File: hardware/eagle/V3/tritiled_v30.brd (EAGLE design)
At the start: 25.4 x 25.4 mm, 12 parts, among them IC1 PIC12LF1571

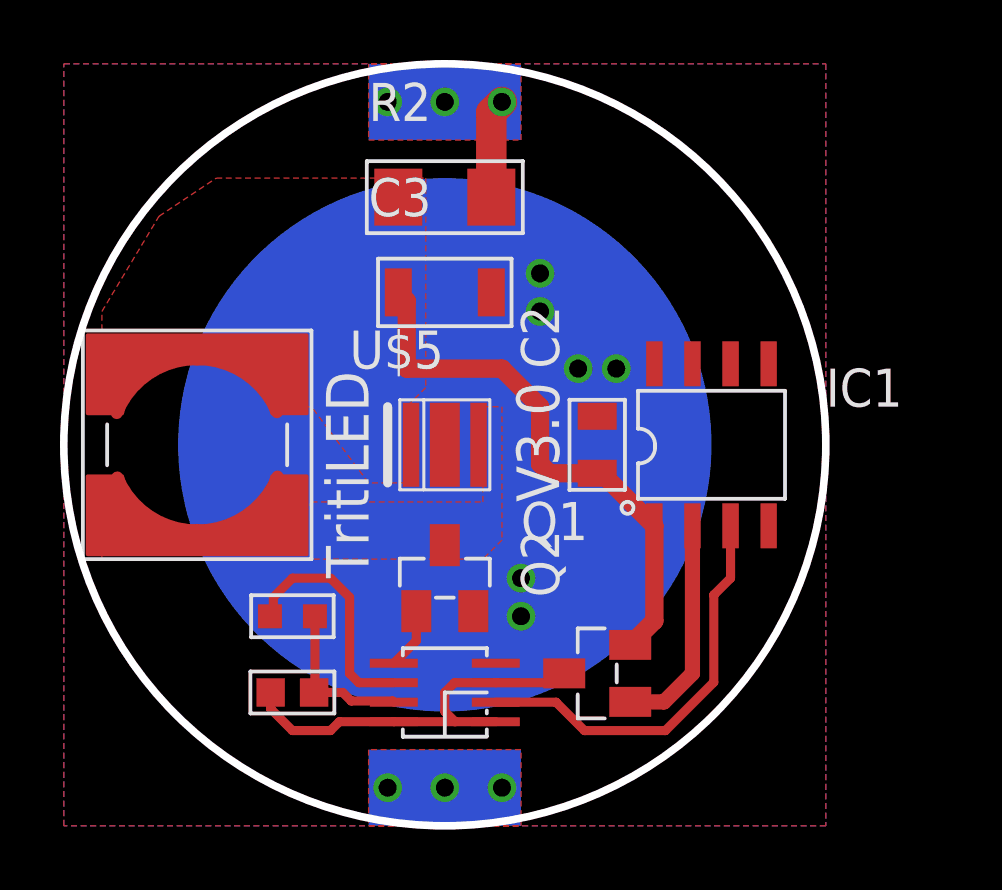
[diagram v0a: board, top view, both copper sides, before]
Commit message: Fixed V3.0 board (74LVC1G123 A_bar now pulled low)
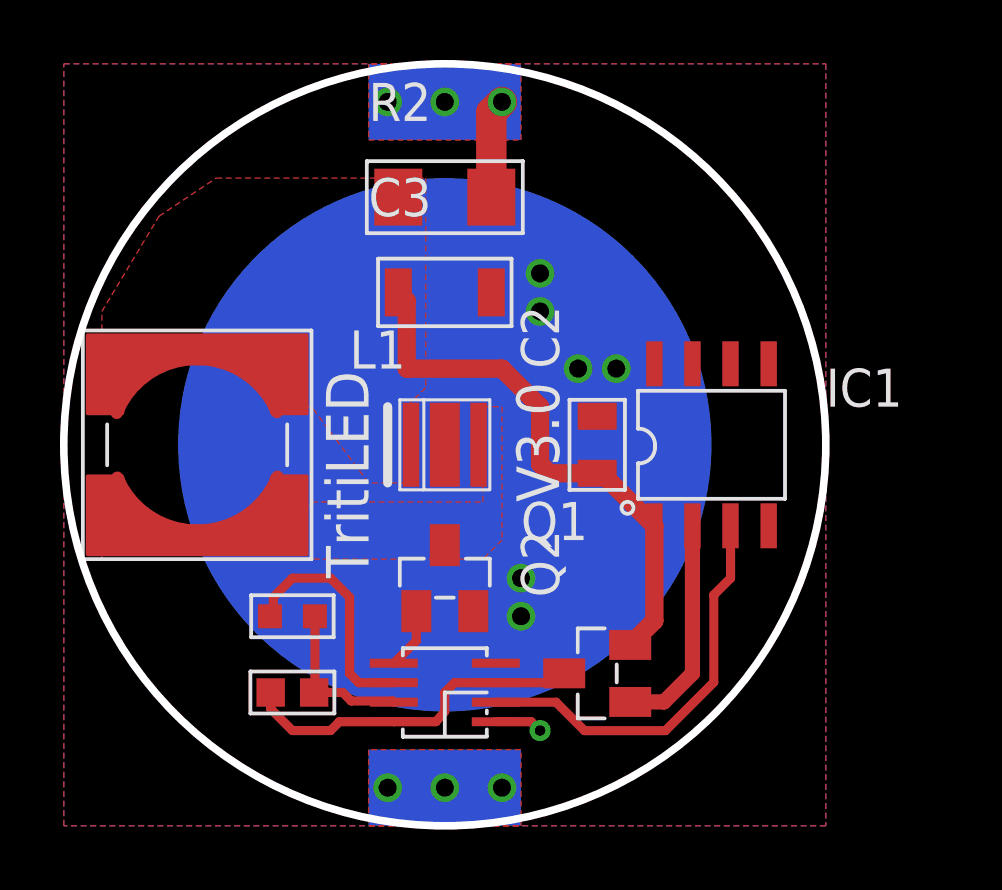
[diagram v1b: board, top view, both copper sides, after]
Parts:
- C2: value (none) -> 100n
- C3: value (none) -> 10u
- C5: value (none) -> 100p
- L1: value (none) -> 1m
- Q1: value (none) -> IRLML6244
- Q2: value (none) -> DMG2305UX
- R2: value (none) -> 100
- R3: value (none) -> 10k
- U$1: value OSLON_SIGNAL -> Oslon Signal Verde
- renumbered U$17 to IC2, U$2 to B1, U$5 to L1
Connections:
- net GND: now also IC2.1
- net N$7: no longer IC2.1
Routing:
- net N$7: track 13.8 -> 11.8 mm
- net GND: track 0.00 -> 1.60 mm, vias 6 -> 7
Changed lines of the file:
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@@
 </autorouter>
 <elements>
-<element name="C2" library="tritiled" package="0805" value="" x="17.78" y="12.7" rot="R90"/>
+<element name="C2" library="tritiled" package="0805" value="100n" x="17.78" y="12.7" rot="R90"/>
 <element name="IC1" library="tritiled" package="SOIC8" value="PIC12LF1571" x="21.59" y="12.7"/>
-<element name="Q1" library="tritiled" package="SOT-23" value="" x="12.7" y="8.255"/>
-<element name="U$1" library="tritiled" package="OSLON_3030_LED" value="OSLON_SIGNAL" x="12.7" y="12.7" rot="R180"/>
-<element name="U$2" library="tritiled" package="CR2032_BAT-HLD_001" value="BAT-HLD-001_CR2032" x="12.7" y="12.7" rot="MR270"/>
-<element name="U$5" library="tritiled" package="SRR6028_INDUCTOR" value="" x="4.445" y="12.7"/>
-<element name="R2" library="tritiled" package="R1206" value="" x="12.7" y="20.955"/>
-<element name="C3" library="tritiled" package="1206" value="" x="12.7" y="17.78"/>
-<element name="U$17" library="tritiled" package="SM8" value="74LVC1G123" x="12.7" y="4.445" rot="R90"/>
-<element name="R3" library="tritiled" package="R0603" value="" x="7.62" y="4.445" rot="R180"/>
-<element name="C5" library="tritiled" package="C0603" value="" x="7.62" y="6.985" rot="R180"/>
-<element name="Q2" library="tritiled" package="SOT-23" value="" x="17.78" y="5.08" rot="R90"/>
+<element name="Q1" library="tritiled" package="SOT-23" value="IRLML6244" x="12.7" y="8.255"/>
+<element name="U$1" library="tritiled" package="OSLON_3030_LED" value="Oslon Signal Verde" x="12.7" y="12.7" rot="R180"/>
+<element name="B1" library="tritiled" package="CR2032_BAT-HLD_001" value="BAT-HLD-001_CR2032" x="12.7" y="12.7" rot="MR270"/>
+<element name="L1" library="tritiled" package="SRR6028_INDUCTOR" value="1m" x="4.445" y="12.7"/>
+<element name="R2" library="tritiled" package="R1206" value="100" x="12.7" y="20.955"/>
+<element name="C3" library="tritiled" package="1206" value="10u" x="12.7" y="17.78"/>
+<element name="IC2" library="tritiled" package="SM8" value="74LVC1G123" x="12.7" y="4.445" rot="R90"/>
+<element name="R3" library="tritiled" package="R0603" value="10k" x="7.62" y="4.445" rot="R180"/>
+<element name="C5" library="tritiled" package="C0603" value="100p" x="7.62" y="6.985" rot="R180"/>
+<element name="Q2" library="tritiled" package="SOT-23" value="DMG2305UX" x="17.78" y="5.08" rot="R90"/>
 </elements>
 <signals>
 <signal name="+3.6V">
-<contactref element="U$5" pad="P$1"/>
+<contactref element="L1" pad="P$1"/>
 <contactref element="U$1" pad="C"/>
 <contactref element="IC1" pad="1"/>
@@
 <contactref element="Q1" pad="2"/>
 <contactref element="IC1" pad="8"/>
-<contactref element="U$2" pad="GND"/>
+<contactref element="B1" pad="GND"/>
 <contactref element="C2" pad="P$2"/>
 <contactref element="C3" pad="P$2"/>
@@
 <vertex x="25.4" y="0"/>
 </polygon>
-<contactref element="U$17" pad="4"/>
+<contactref element="IC2" pad="4"/>
 <via x="17.145" y="15.24" extent="1-16" drill="0.6"/>
 <via x="18.415" y="15.24" extent="1-16" drill="0.6"/>
@@
 <via x="15.875" y="18.415" extent="1-16" drill="0.6"/>
 <via x="15.875" y="17.145" extent="1-16" drill="0.6"/>
+<contactref element="IC2" pad="1"/>
+<wire x1="14.4" y1="3.47" x2="15.58" y2="3.47" width="0.3048" layer="1"/>
+<wire x1="15.58" y1="3.47" x2="15.875" y2="3.175" width="0.3048" layer="1"/>
+<via x="15.875" y="3.175" extent="1-16" drill="0.35"/>
 </signal>
 <signal name="N$9">
-<contactref element="U$2" pad="+V1" route="any" routetag="G$1.+V"/>
+<contactref element="B1" pad="+V1" route="any" routetag="G$1.+V"/>
 <contactref element="R2" pad="P$2"/>
-<contactref element="U$2" pad="+V2" route="any" routetag="G$1.+V"/>
+<contactref element="B1" pad="+V2" route="any" routetag="G$1.+V"/>
 <polygon width="0.254" layer="1" orphans="yes" thermals="no">
 <vertex x="10.16" y="25.4"/>
@@
 </signal>
 <signal name="N$10">
-<contactref element="U$5" pad="P$2"/>
+<contactref element="L1" pad="P$2"/>
 <contactref element="Q1" pad="3"/>
 <contactref element="U$1" pad="A"/>
@@
 <contactref element="R3" pad="P$1"/>
 <contactref element="C5" pad="P$1"/>
-<contactref element="U$17" pad="7"/>
+<contactref element="IC2" pad="7"/>
 <wire x1="11" y1="4.12" x2="10.9596" y2="4.1604" width="0.3048" layer="1"/>
 <wire x1="9.58249375" y1="4.1604" x2="9.29789375" y2="4.445" width="0.3048" layer="1"/>
@@
 </signal>
 <signal name="N$5">
-<contactref element="U$17" pad="6"/>
+<contactref element="IC2" pad="6"/>
 <contactref element="C5" pad="P$2"/>
 <wire x1="11" y1="4.77" x2="9.835" y2="4.77" width="0.3048" layer="1"/>
@@
 </signal>
 <signal name="N$7">
-<contactref element="U$17" pad="8"/>
+<contactref element="IC2" pad="8"/>
 <contactref element="R3" pad="P$2"/>
 <contactref element="Q2" pad="3"/>
-<contactref element="U$17" pad="3"/>
-<contactref element="U$17" pad="1"/>
+<contactref element="IC2" pad="3"/>
 <wire x1="16.37" y1="4.77" x2="14.4" y2="4.77" width="0.3048" layer="1"/>
 <wire x1="16.37" y1="4.77" x2="16.68" y2="5.08" width="0.3048" layer="1"/>
@@
 <wire x1="13.025" y1="4.77" x2="12.7" y2="4.445" width="0.3048" layer="1"/>
 <wire x1="12.7" y1="4.445" x2="12.7" y2="3.81" width="0.3048" layer="1"/>
-<wire x1="12.7" y1="3.81" x2="13.04" y2="3.47" width="0.3048" layer="1"/>
-<wire x1="13.04" y1="3.47" x2="11" y2="3.47" width="0.3048" layer="1"/>
-<wire x1="13.04" y1="3.47" x2="14.4" y2="3.47" width="0.3048" layer="1"/>
+<wire x1="12.7" y1="3.81" x2="12.405" y2="3.47" width="0.3048" layer="1"/>
+<wire x1="12.405" y1="3.47" x2="11" y2="3.47" width="0.3048" layer="1"/>
 <wire x1="11" y1="3.47" x2="9.185" y2="3.47" width="0.3048" layer="1"/>
 <wire x1="9.185" y1="3.47" x2="8.89" y2="3.175" width="0.3048" layer="1"/>
@@
 </signal>
 <signal name="N$2">
-<contactref element="U$17" pad="5"/>
+<contactref element="IC2" pad="5"/>
 <contactref element="Q1" pad="1"/>
 <wire x1="11" y1="5.42" x2="11.75" y2="6.17" width="0.3048" layer="1"/>
@@
 <signal name="N$4">
 <contactref element="IC1" pad="3"/>
-<contactref element="U$17" pad="2"/>
+<contactref element="IC2" pad="2"/>
 <wire x1="21.6662" y1="7.6962" x2="22.225" y2="8.255" width="0.3048" layer="1"/>
 <wire x1="21.6662" y1="4.78540625" x2="21.6662" y2="7.6962" width="0.3048" layer="1"/>
